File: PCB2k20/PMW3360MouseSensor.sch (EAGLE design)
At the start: 10 parts

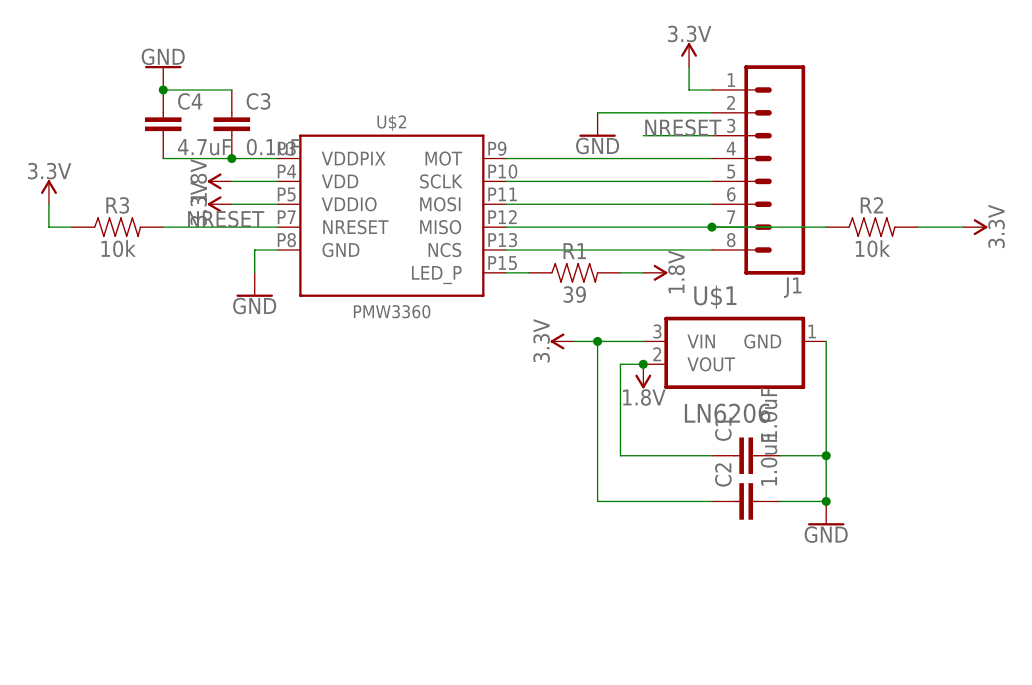
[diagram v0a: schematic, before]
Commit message: Finalise PMW3360 breakout - done pin markings and cleanup - swapped position of some pins to route stuff more easily
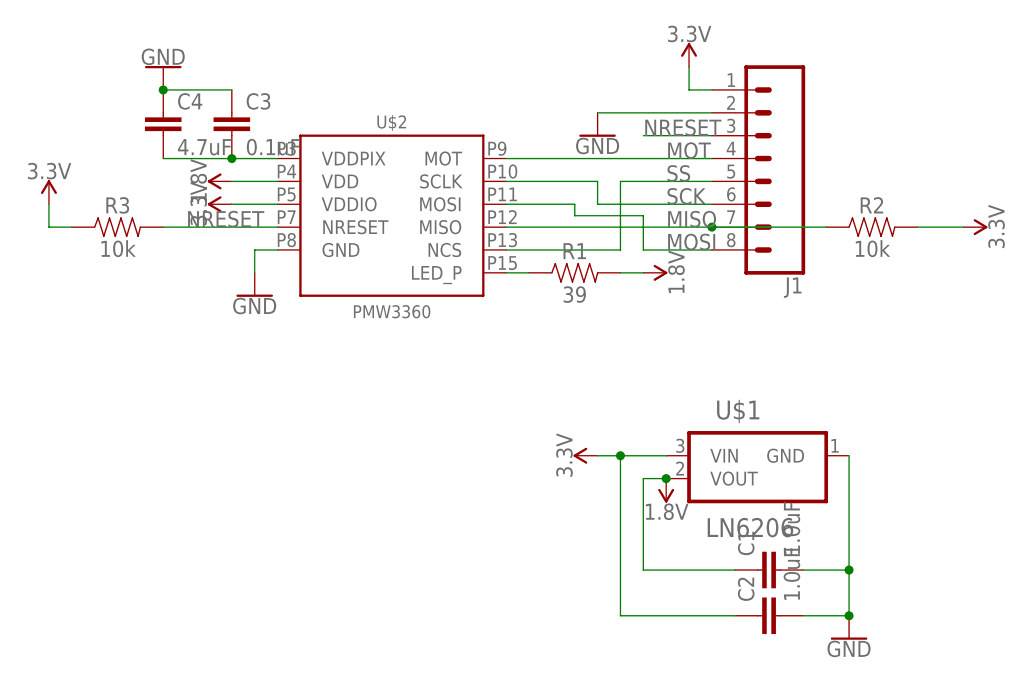
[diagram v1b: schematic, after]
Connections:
- net N$42 renamed MISO
- net N$47 renamed MOT
- removed net N$40: J1.8, U$2.NCS
- removed net N$45: J1.6, U$2.MOSI
- removed net N$46: J1.5, U$2.SCLK
- new net MOSI: J1.8, U$2.MOSI
- new net SCK: J1.6, U$2.SCLK
- new net SS: J1.5, U$2.NCS
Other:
- moved on the sheet: C1, C2, U$1
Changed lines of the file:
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@@
 <drawing>
 <settings>
-<setting alwaysvectorfont="yes"/>
+<setting alwaysvectorfont="no"/>
 <setting verticaltext="up"/>
 </settings>
-<grid distance="0.1" unitdist="inch" unit="inch" style="lines" multiple="1" display="no" altdistance="0.01" altunitdist="inch" altunit="inch"/>
+<grid distance="0.1" unitdist="inch" unit="inch" style="lines" multiple="1" display="no" altdistance="0.05" altunitdist="inch" altunit="inch"/>
 <layers>
 <layer number="1" name="Top" color="4" fill="1" visible="no" active="no"/>
@@
 </plain>
 <instances>
-<instance part="U$1" gate="A" x="96.52" y="33.02" smashed="yes">
-<attribute name="NAME" x="91.7897" y="37.06051875" size="2.083790625" layer="95" ratio="10" rot="SR0"/>
-<attribute name="VALUE" x="90.72225" y="23.9899" size="2.08515" layer="96" ratio="10" rot="SR0"/>
+<instance part="U$1" gate="A" x="99.06" y="20.32" smashed="yes">
+<attribute name="NAME" x="94.3297" y="24.36051875" size="2.083790625" layer="95" ratio="10" rot="SR0"/>
+<attribute name="VALUE" x="93.26225" y="11.2899" size="2.08515" layer="96" ratio="10" rot="SR0"/>
 </instance>
 <instance part="U$2" gate="G$1" x="58.42" y="48.26" smashed="yes">
@@
 <attribute name="VALUE" x="58.42" y="36.322" size="1.4224" layer="96" font="vector" ratio="16" align="center"/>
 </instance>
-<instance part="GND24" gate="1" x="106.68" y="12.7" smashed="yes">
-<attribute name="VALUE" x="106.68" y="12.446" size="1.778" layer="96" align="top-center"/>
-</instance>
-<instance part="C1" gate="G$1" x="99.06" y="20.32" smashed="yes" rot="R90">
-<attribute name="NAME" x="96.139" y="21.844" size="1.778" layer="95" font="vector" rot="R90"/>
-<attribute name="VALUE" x="101.219" y="21.844" size="1.778" layer="96" font="vector" rot="R90"/>
-</instance>
-<instance part="C2" gate="G$1" x="99.06" y="15.24" smashed="yes" rot="R90">
-<attribute name="NAME" x="96.139" y="16.764" size="1.778" layer="95" font="vector" rot="R90"/>
-<attribute name="VALUE" x="101.219" y="16.764" size="1.778" layer="96" font="vector" rot="R90"/>
-</instance>
-<instance part="SUPPLY18" gate="G$1" x="86.36" y="30.48" smashed="yes" rot="R180">
-<attribute name="VALUE" x="86.36" y="27.686" size="1.778" layer="96" rot="R180" align="bottom-center"/>
+<instance part="GND24" gate="1" x="109.22" y="0" smashed="yes">
+<attribute name="VALUE" x="109.22" y="-0.254" size="1.778" layer="96" align="top-center"/>
+</instance>
+<instance part="C1" gate="G$1" x="101.6" y="7.62" smashed="yes" rot="R90">
+<attribute name="NAME" x="98.679" y="9.144" size="1.778" layer="95" font="vector" rot="R90"/>
+<attribute name="VALUE" x="103.759" y="9.144" size="1.778" layer="96" font="vector" rot="R90"/>
+</instance>
+<instance part="C2" gate="G$1" x="101.6" y="2.54" smashed="yes" rot="R90">
+<attribute name="NAME" x="98.679" y="4.064" size="1.778" layer="95" font="vector" rot="R90"/>
+<attribute name="VALUE" x="103.759" y="4.064" size="1.778" layer="96" font="vector" rot="R90"/>
+</instance>
+<instance part="SUPPLY18" gate="G$1" x="88.9" y="17.78" smashed="yes" rot="R180">
+<attribute name="VALUE" x="88.9" y="14.986" size="1.778" layer="96" rot="R180" align="bottom-center"/>
 </instance>
 <instance part="SUPPLY24" gate="G$1" x="40.64" y="50.8" smashed="yes" rot="R90">
@@
 <attribute name="VALUE" x="89.154" y="40.64" size="1.778" layer="96" rot="R270" align="bottom-center"/>
 </instance>
-<instance part="SUPPLY34" gate="G$1" x="78.74" y="33.02" smashed="yes" rot="R90">
-<attribute name="VALUE" x="75.946" y="33.02" size="1.778" layer="96" rot="R90" align="bottom-center"/>
+<instance part="SUPPLY34" gate="G$1" x="81.28" y="20.32" smashed="yes" rot="R90">
+<attribute name="VALUE" x="78.486" y="20.32" size="1.778" layer="96" rot="R90" align="bottom-center"/>
 </instance>
 <instance part="GND25" gate="1" x="43.18" y="38.1" smashed="yes">
@@
 <pinref part="U$1" gate="A" pin="GND"/>
 <pinref part="GND24" gate="1" pin="GND"/>
-<wire x1="106.68" y1="15.24" x2="106.68" y2="20.32" width="0.1524" layer="91"/>
+<wire x1="109.22" y1="2.54" x2="109.22" y2="7.62" width="0.1524" layer="91"/>
 <pinref part="C2" gate="G$1" pin="2"/>
-<wire x1="106.68" y1="20.32" x2="106.68" y2="33.02" width="0.1524" layer="91"/>
-<wire x1="101.6" y1="15.24" x2="106.68" y2="15.24" width="0.1524" layer="91"/>
-<junction x="106.68" y="15.24"/>
+<wire x1="109.22" y1="7.62" x2="109.22" y2="20.32" width="0.1524" layer="91"/>
+<wire x1="104.14" y1="2.54" x2="109.22" y2="2.54" width="0.1524" layer="91"/>
+<junction x="109.22" y="2.54"/>
 <pinref part="C1" gate="G$1" pin="2"/>
-<wire x1="101.6" y1="20.32" x2="106.68" y2="20.32" width="0.1524" layer="91"/>
-<junction x="106.68" y="20.32"/>
+<wire x1="104.14" y1="7.62" x2="109.22" y2="7.62" width="0.1524" layer="91"/>
+<junction x="109.22" y="7.62"/>
 </segment>
 <segment>
@@
 <segment>
 <pinref part="U$1" gate="A" pin="VOUT"/>
-<wire x1="86.36" y1="30.48" x2="83.82" y2="30.48" width="0.1524" layer="91"/>
-<wire x1="83.82" y1="30.48" x2="83.82" y2="20.32" width="0.1524" layer="91"/>
+<wire x1="88.9" y1="17.78" x2="86.36" y2="17.78" width="0.1524" layer="91"/>
+<wire x1="86.36" y1="17.78" x2="86.36" y2="7.62" width="0.1524" layer="91"/>
 <pinref part="C1" gate="G$1" pin="1"/>
-<wire x1="83.82" y1="20.32" x2="93.98" y2="20.32" width="0.1524" layer="91"/>
+<wire x1="86.36" y1="7.62" x2="96.52" y2="7.62" width="0.1524" layer="91"/>
 <pinref part="SUPPLY18" gate="G$1" pin="1.8V"/>
-<junction x="86.36" y="30.48"/>
+<junction x="88.9" y="17.78"/>
 </segment>
 <segment>
@@
 <segment>
 <pinref part="U$1" gate="A" pin="VIN"/>
-<wire x1="86.36" y1="33.02" x2="81.28" y2="33.02" width="0.1524" layer="91"/>
-<wire x1="81.28" y1="33.02" x2="78.74" y2="33.02" width="0.1524" layer="91"/>
+<wire x1="88.9" y1="20.32" x2="83.82" y2="20.32" width="0.1524" layer="91"/>
+<wire x1="83.82" y1="20.32" x2="81.28" y2="20.32" width="0.1524" layer="91"/>
 <pinref part="C2" gate="G$1" pin="1"/>
-<wire x1="81.28" y1="15.24" x2="93.98" y2="15.24" width="0.1524" layer="91"/>
+<wire x1="83.82" y1="2.54" x2="96.52" y2="2.54" width="0.1524" layer="91"/>
 <pinref part="SUPPLY34" gate="G$1" pin="3.3V"/>
-<wire x1="81.28" y1="15.24" x2="81.28" y2="33.02" width="0.1524" layer="91"/>
-<junction x="81.28" y="33.02"/>
+<wire x1="83.82" y1="2.54" x2="83.82" y2="20.32" width="0.1524" layer="91"/>
+<junction x="83.82" y="20.32"/>
 </segment>
 <segment>
@@
 </segment>
 </net>
-<net name="N$40" class="0">
-<segment>
-<pinref part="U$2" gate="G$1" pin="NCS"/>
-<wire x1="71.12" y1="43.18" x2="93.98" y2="43.18" width="0.1524" layer="91"/>
-<pinref part="J1" gate="G$1" pin="8"/>
-</segment>
-</net>
-<net name="N$42" class="0">
-<segment>
-<pinref part="U$2" gate="G$1" pin="MISO"/>
+<net name="MISO" class="0">
+<segment>
 <wire x1="106.68" y1="45.72" x2="93.98" y2="45.72" width="0.1524" layer="91"/>
 <pinref part="R2" gate="G$1" pin="1"/>
 <pinref part="J1" gate="G$1" pin="7"/>
-<wire x1="93.98" y1="45.72" x2="71.12" y2="45.72" width="0.1524" layer="91"/>
+<pinref part="U$2" gate="G$1" pin="MISO"/>
+<wire x1="71.12" y1="45.72" x2="93.98" y2="45.72" width="0.1524" layer="91"/>
 <junction x="93.98" y="45.72"/>
-</segment>
-</net>
-<net name="N$45" class="0">
-<segment>
-<pinref part="U$2" gate="G$1" pin="MOSI"/>
-<wire x1="71.12" y1="48.26" x2="93.98" y2="48.26" width="0.1524" layer="91"/>
-<pinref part="J1" gate="G$1" pin="6"/>
-</segment>
-</net>
-<net name="N$46" class="0">
-<segment>
-<pinref part="U$2" gate="G$1" pin="SCLK"/>
-<wire x1="93.98" y1="50.8" x2="71.12" y2="50.8" width="0.1524" layer="91"/>
-<pinref part="J1" gate="G$1" pin="5"/>
-</segment>
-</net>
-<net name="N$47" class="0">
+<label x="88.9" y="45.72" size="1.778" layer="95"/>
+</segment>
+</net>
+<net name="MOT" class="0">
 <segment>
 <pinref part="U$2" gate="G$1" pin="MOT"/>
 <wire x1="71.12" y1="53.34" x2="93.98" y2="53.34" width="0.1524" layer="91"/>
 <pinref part="J1" gate="G$1" pin="4"/>
+<label x="88.9" y="53.34" size="1.778" layer="95"/>
 </segment>
 </net>
@@
 </segment>
 </net>
+<net name="SS" class="0">
+<segment>
+<pinref part="U$2" gate="G$1" pin="NCS"/>
+<wire x1="71.12" y1="43.18" x2="83.82" y2="43.18" width="0.1524" layer="91"/>
+<wire x1="83.82" y1="43.18" x2="83.82" y2="50.8" width="0.1524" layer="91"/>
+<pinref part="J1" gate="G$1" pin="5"/>
+<wire x1="83.82" y1="50.8" x2="93.98" y2="50.8" width="0.1524" layer="91"/>
+<label x="88.9" y="50.8" size="1.778" layer="95"/>
+</segment>
+</net>
+<net name="SCK" class="0">
+<segment>
+<pinref part="U$2" gate="G$1" pin="SCLK"/>
+<wire x1="71.12" y1="50.8" x2="81.28" y2="50.8" width="0.1524" layer="91"/>
+<wire x1="81.28" y1="50.8" x2="81.28" y2="48.26" width="0.1524" layer="91"/>
+<pinref part="J1" gate="G$1" pin="6"/>
+<wire x1="81.28" y1="48.26" x2="93.98" y2="48.26" width="0.1524" layer="91"/>
+<label x="88.9" y="48.26" size="1.778" layer="95"/>
+</segment>
+</net>
+<net name="MOSI" class="0">
+<segment>
+<pinref part="U$2" gate="G$1" pin="MOSI"/>
+<wire x1="71.12" y1="48.26" x2="78.74" y2="48.26" width="0.1524" layer="91"/>
+<wire x1="78.74" y1="48.26" x2="78.74" y2="46.99" width="0.1524" layer="91"/>
+<wire x1="78.74" y1="46.99" x2="86.36" y2="46.99" width="0.1524" layer="91"/>
+<wire x1="86.36" y1="46.99" x2="86.36" y2="43.18" width="0.1524" layer="91"/>
+<pinref part="J1" gate="G$1" pin="8"/>
+<wire x1="86.36" y1="43.18" x2="93.98" y2="43.18" width="0.1524" layer="91"/>
+<label x="88.9" y="43.18" size="1.778" layer="95"/>
+</segment>
+</net>
